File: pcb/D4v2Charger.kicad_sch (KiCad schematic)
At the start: 14 parts, among them J1 Conn_01x02_Pin, U1 BQ25185DLHR

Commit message: updates & license addition
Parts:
- added D3: D_Schottky, PMEG1020EJ_115:DIO_PMEG6010CEJF, symbol Device:D_Schottky
- added F1: Polyfuse, Littlefuse_0406L:0402L100SLKR, symbol Device:Polyfuse
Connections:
- net VBUS: now also D3.1 (K); no longer J1.1 (Pin_1)
- new net: D3.2 (A), F1.1
- new net: F1.2, J1.1 (Pin_1)
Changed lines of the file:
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@@
-	)
-	(junction
-		(at 24.13 104.14)
-		(diameter 0)
-		(color 0 0 0 0)
 	)
 	(junction
@@
 		(color 0 0 0 0)
 	)
+	(junction
+		(at 26.67 104.14)
+		(diameter 0)
+		(color 0 0 0 0)
+	)
 	(wire
 		(pts
@@
 	(wire
 		(pts
+			(xy 38.1 104.14) (xy 45.72 104.14)
+		)
+		(stroke
+			(width 0)
+			(type default)
+		)
+	)
+	(wire
+		(pts
 			(xy 60.96 58.42) (xy 60.96 73.66)
 		)
@@
 	(wire
 		(pts
+			(xy 59.69 104.14) (xy 59.69 111.76)
+		)
+		(stroke
+			(width 0)
+			(type default)
+		)
+	)
+	(wire
+		(pts
+			(xy 30.48 104.14) (xy 26.67 104.14)
+		)
+		(stroke
+			(width 0)
+			(type default)
+		)
+	)
+	(wire
+		(pts
 			(xy 96.52 40.64) (xy 101.6 40.64)
 		)
@@
 	(wire
 		(pts
-			(xy 24.13 104.14) (xy 24.13 105.41)
-		)
-		(stroke
-			(width 0)
-			(type default)
-		)
-	)
-	(wire
-		(pts
 			(xy 24.13 40.64) (xy 24.13 45.72)
 		)
@@
 	(wire
 		(pts
-			(xy 24.13 104.14) (xy 59.69 104.14)
-		)
-		(stroke
-			(width 0)
-			(type default)
-		)
-	)
-	(wire
-		(pts
-			(xy 59.69 104.14) (xy 59.69 111.76)
+			(xy 53.34 104.14) (xy 59.69 104.14)
 		)
 		(stroke
@@
 	(wire
 		(pts
-			(xy 24.13 105.41) (xy 26.67 105.41)
+			(xy 24.13 104.14) (xy 26.67 104.14)
 		)
 		(stroke
@@
 	(wire
 		(pts
-			(xy 26.67 109.22) (xy 26.67 105.41)
+			(xy 26.67 104.14) (xy 26.67 109.22)
 		)
 		(stroke
@@
 	)
 	(symbol
+		(lib_id "Device:Polyfuse")
+		(at 49.53 104.14 90)
+		(unit 1)
+		(exclude_from_sim no)
+		(in_bom yes)
+		(on_board yes)
+		(dnp no)
+		(fields_autoplaced yes)
+		(property "Reference" "F1"
+			(at 49.53 97.79 90)
+			(effects
+				(font
+					(size 1.27 1.27)
+				)
+			)
+		)
+		(property "Value" "Polyfuse"
+			(at 49.53 100.33 90)
+			(effects
+				(font
+					(size 1.27 1.27)
+				)
+			)
+		)
+		(property "Footprint" "Littlefuse_0406L:0402L100SLKR"
+			(at 54.61 102.87 0)
+			(effects
+				(font
+					(size 1.27 1.27)
+				)
+				(justify left)
+				(hide yes)
+			)
+		)
+		(property "Datasheet" "~"
+			(at 49.53 104.14 0)
+			(effects
+				(font
+					(size 1.27 1.27)
+				)
+				(hide yes)
+			)
+		)
+		(property "Description" "Resettable fuse, polymeric positive temperature coefficient"
+			(at 49.53 104.14 0)
+			(effects
+				(font
+					(size 1.27 1.27)
+				)
+				(hide yes)
+			)
+		)
+		(pin "2"
+		)
+		(pin "1"
+		)
+		(instances
+			(project ""
+				(path "/88573ec5-2eb3-489f-b9be-0922d5590a50"
+					(reference "F1")
+					(unit 1)
+				)
+			)
+		)
+	)
+	(symbol
 		(lib_id "power:GND")
 		(at 132.08 58.42 0)
@@
 					(unit 1)
 				)
+			)
+		)
+	)
+	(symbol
+		(lib_id "Device:D_Schottky")
+		(at 34.29 104.14 0)
+		(unit 1)
+		(exclude_from_sim no)
+		(in_bom yes)
+		(on_board yes)
+		(dnp no)
+		(fields_autoplaced yes)
+		(property "Reference" "D3"
+			(at 33.9725 97.79 0)
+			(effects
+				(font
+					(size 1.27 1.27)
+				)
+			)
+		)
+		(property "Value" "D_Schottky"
+			(at 33.9725 100.33 0)
+			(effects
+				(font
+					(size 1.27 1.27)
+				)
+			)
+		)
+		(property "Footprint" "PMEG1020EJ_115:DIO_PMEG6010CEJF"
+			(at 34.29 104.14 0)
+			(effects
+				(font
+					(size 1.27 1.27)
+				)
+				(hide yes)
+			)
+		)
+		(property "Datasheet" "~"
+			(at 34.29 104.14 0)
+			(effects
+				(font
+					(size 1.27 1.27)
+				)
+				(hide yes)
+			)
+		)
+		(property "Description" "Schottky diode"
+			(at 34.29 104.14 0)
+			(effects
+				(font
+					(size 1.27 1.27)
+				)
+				(hide yes)
+			)
+		)
+		(pin "2"
+		)
+		(pin "1"
+		)
+		(instances
+			(project ""
+				(path "/88573ec5-2eb3-489f-b9be-0922d5590a50"
+					(reference "D3")
+					(unit 1)
+				)

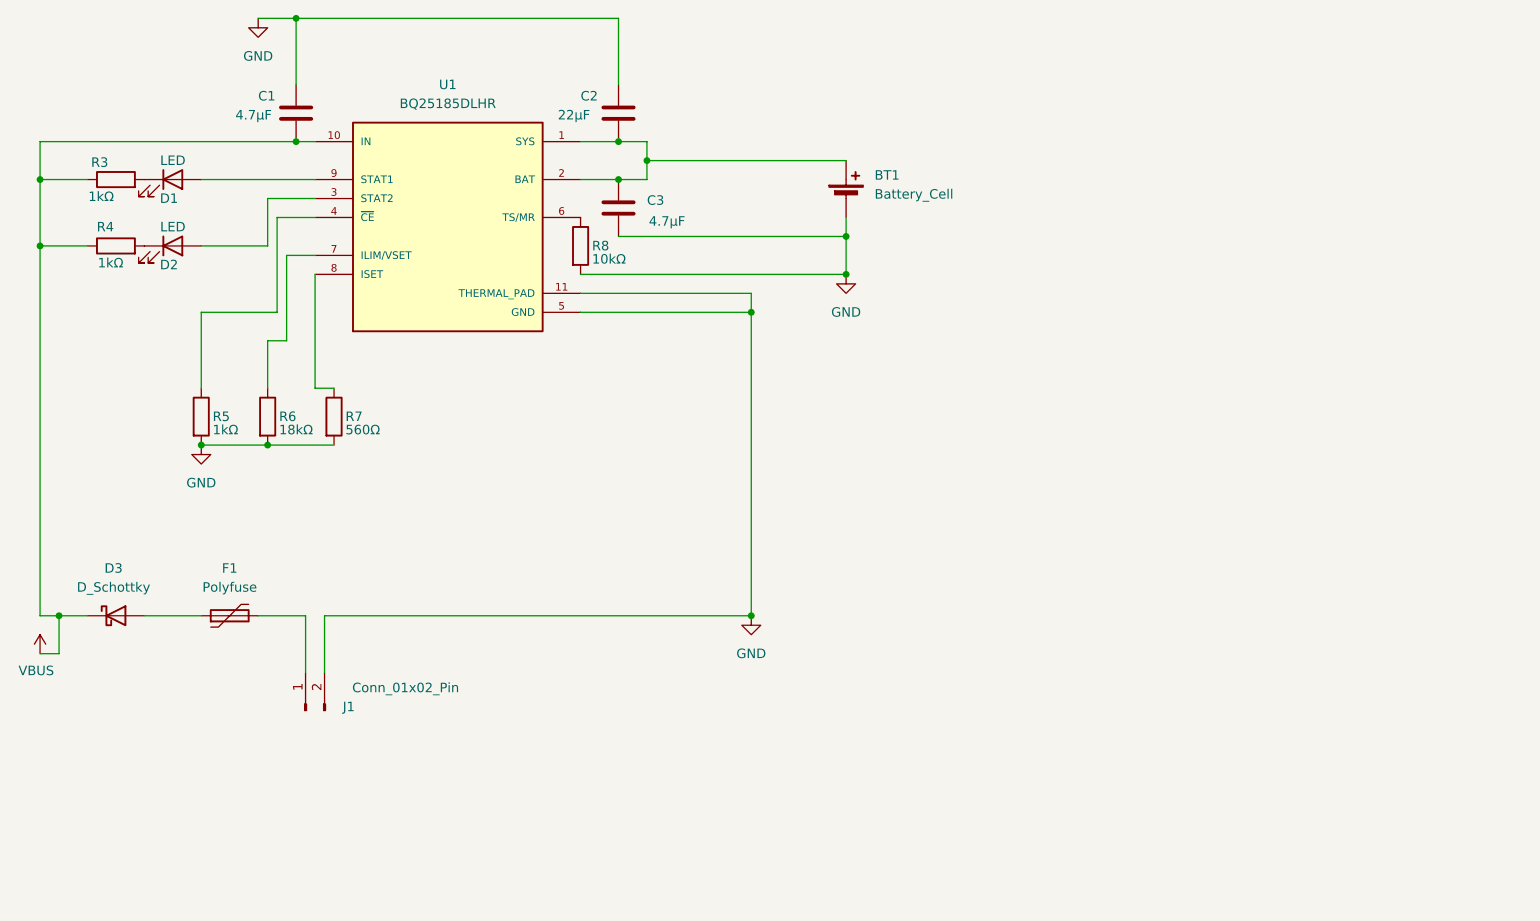
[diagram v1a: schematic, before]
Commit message: updated pcb clearance for magnetic charger
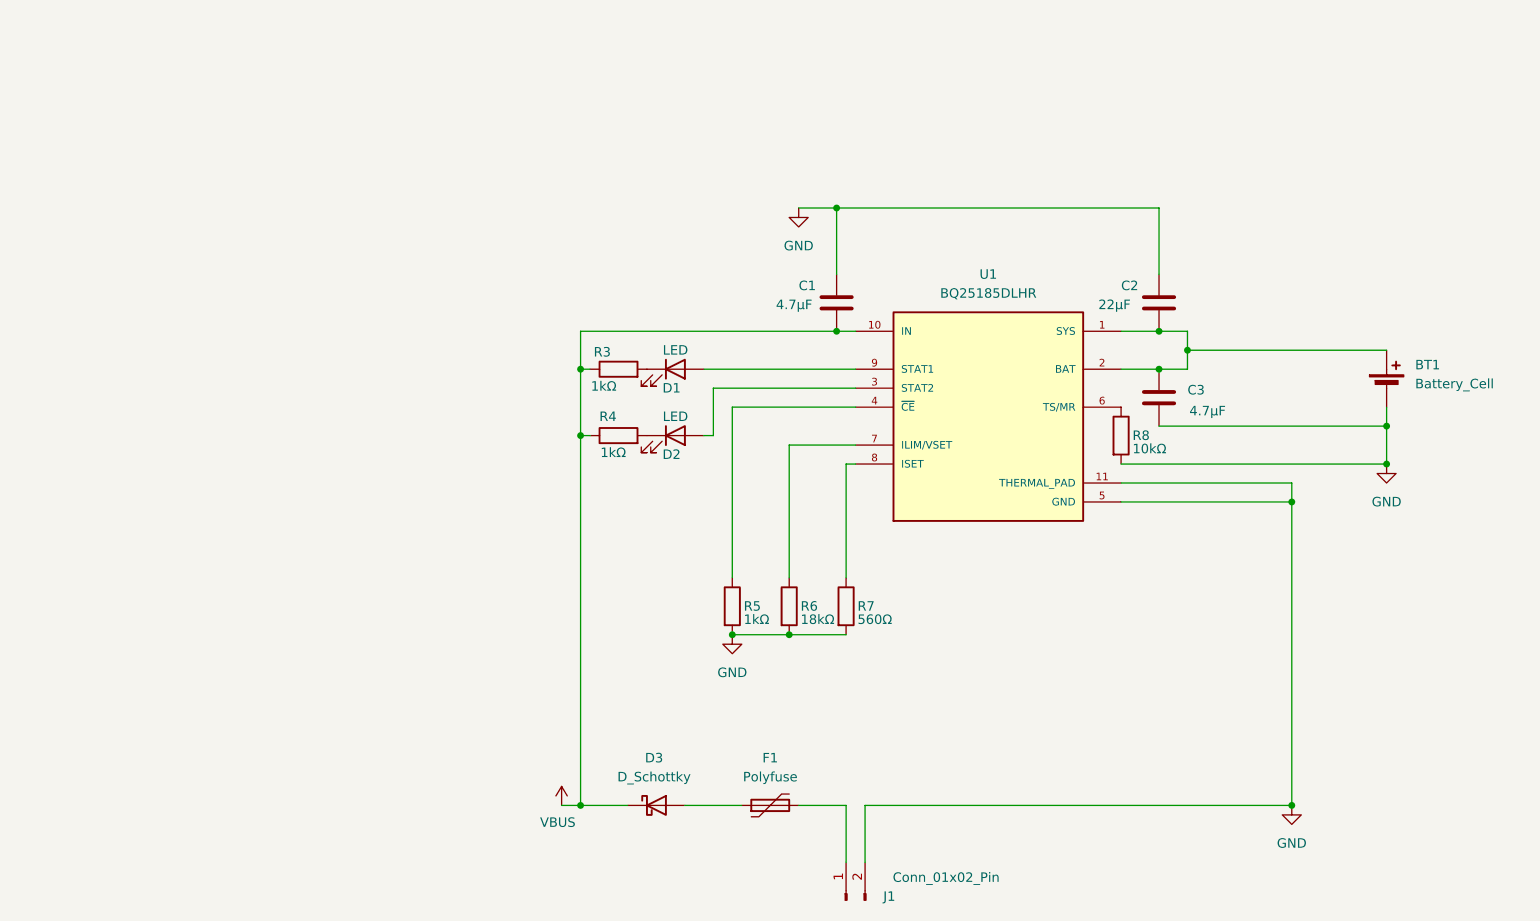
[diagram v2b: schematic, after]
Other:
- title: (none) -> Bat Charger Emisar D4v2
- moved on the sheet: BT1, C1, C2, C3, D1, D2, D3, F1, J1, R3, R4, R5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
